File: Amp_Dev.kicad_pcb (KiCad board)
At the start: 2 copper layers, 100 x 100 mm, 86 parts, among them J1 SMA, J10 SMA, J11 CONN_01X02, J13 SMA, J2 SMA, J20 SMA, J21 SMA, J22 SMA, Q1 DMN2075U, U1 MML09211H, U4 SN74LVC1G17, U5 TLV702, U6 LTC2644, U7 RT9183

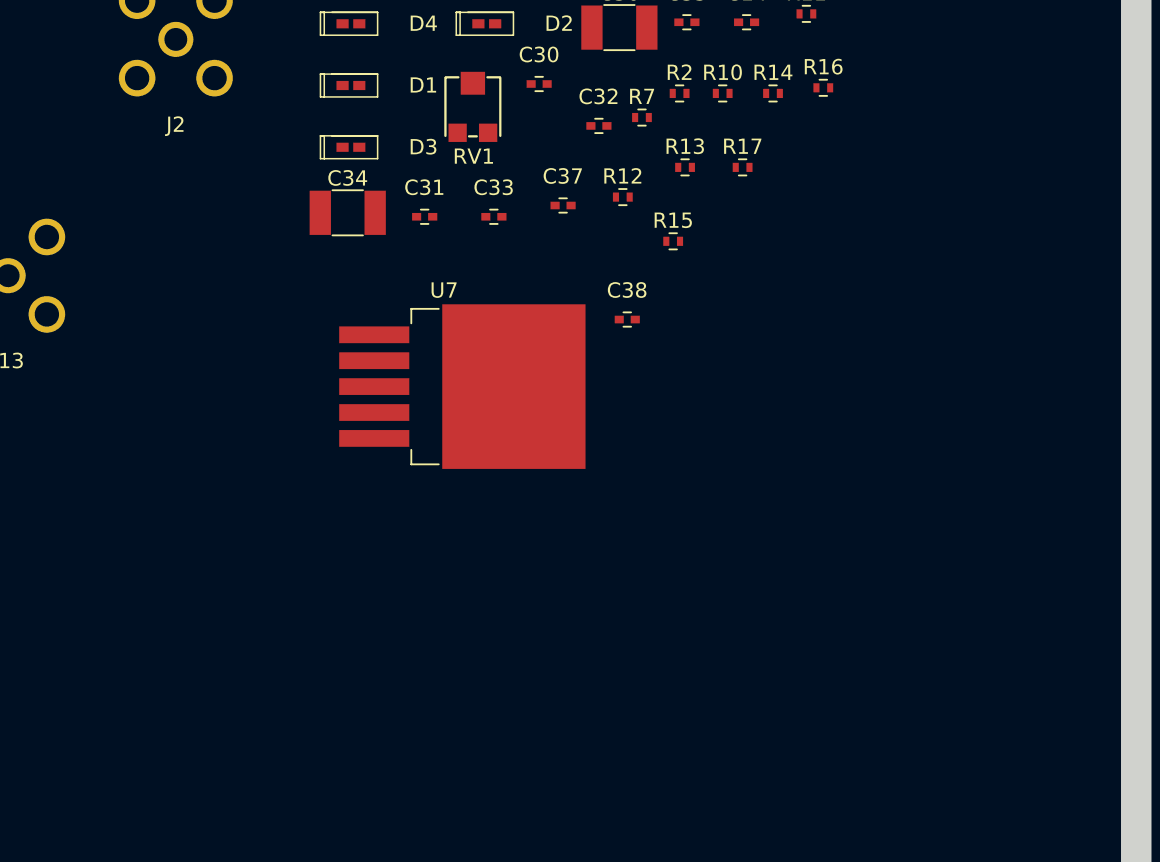
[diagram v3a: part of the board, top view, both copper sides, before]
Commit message: Forward annotated more PA components
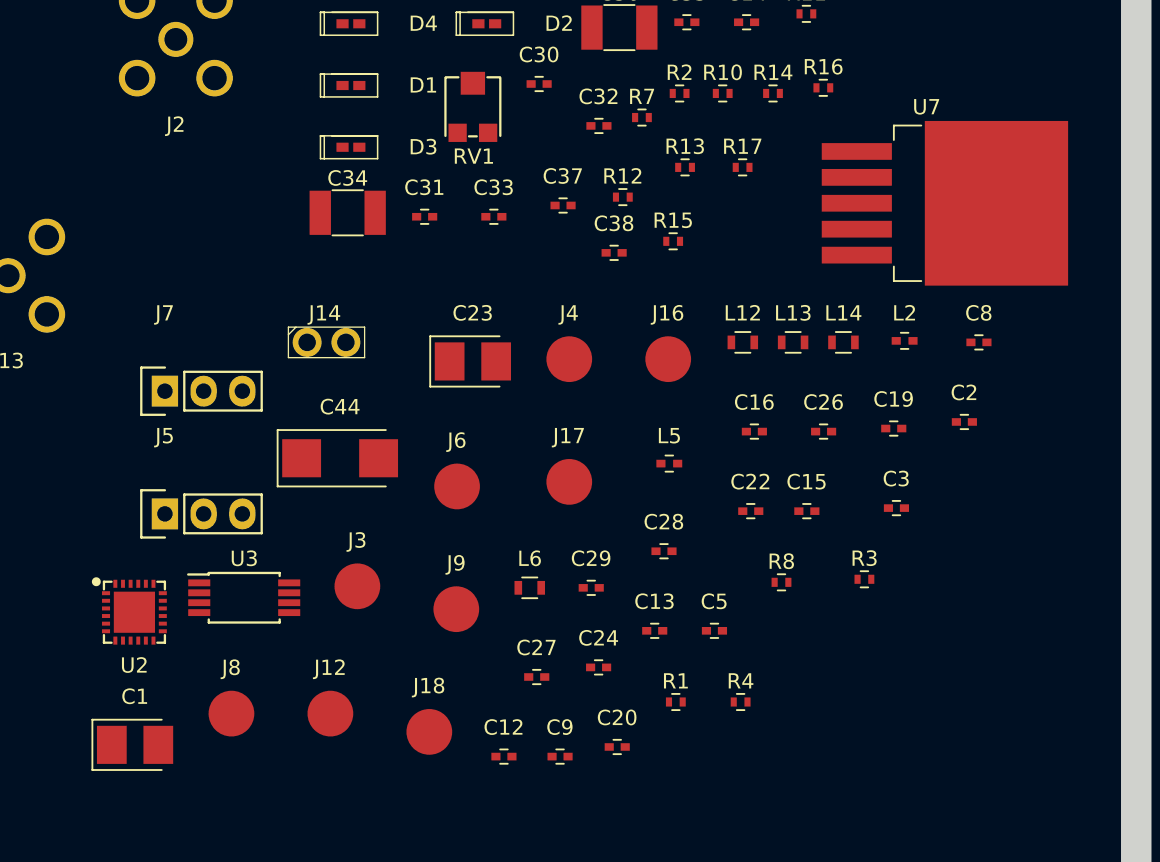
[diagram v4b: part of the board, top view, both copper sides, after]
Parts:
- added C1: 10uF, SFUSat:CP_Tantalum_Case-B_EIA-1411-21_Reflow, F.Cu at (134.3, 102.0)
- added C12: 1uF, SFUSat:C_0402, F.Cu at (158.5, 102.8)
- added C13: 1uF, SFUSat:C_0402, F.Cu at (168.4, 94.5)
- added C15: 1uF, SFUSat:C_0402, F.Cu at (178.4, 86.7)
- added C16: 2.2uF, SFUSat:C_0402, F.Cu at (175.0, 81.5)
- added C19: 1uF, SFUSat:C_0402, F.Cu at (184.1, 81.3)
- added C2: 1uF, SFUSat:C_0402, F.Cu at (188.7, 80.8)
- added C20: DNP, SFUSat:C_0402, F.Cu at (166.0, 102.2)
- added C22: 10pF, SFUSat:C_0402, F.Cu at (174.7, 86.7)
- added C23: 10uF, SFUSat:CP_Tantalum_Case-B_EIA-1411-21_Reflow, F.Cu at (156.5, 76.9)
- added C24: 27pF, SFUSat:C_0402, F.Cu at (164.7, 96.9)
- added C26: 2.2uF, SFUSat:C_0402, F.Cu at (179.5, 81.5)
- added C27: 10pF, SFUSat:C_0402, F.Cu at (160.7, 97.6)
- added C28: 1.2pF, SFUSat:C_0402, F.Cu at (169.0, 89.3)
- added C29: 100pF, SFUSat:C_0402, F.Cu at (164.2, 91.7)
- added C3: 100pF, SFUSat:C_0402, F.Cu at (184.3, 86.5)
- added C44: 10uF, SFUSat:CP_Tantalum_Case-C_EIA-2312-28_Reflow, F.Cu at (147.8, 83.2)
- added C5: 2.2uF, SFUSat:C_0402, F.Cu at (172.3, 94.5)
- added C8: 220pF, SFUSat:C_0402, F.Cu at (189.7, 75.6)
- added C9: 22pF, SFUSat:C_0402, F.Cu at (162.2, 102.8)
- added J12: TEST_1P, SFUSat:Measurement_Point_Round-SMD-Pad_Big, F.Cu at (147.1, 100.0)
- added J14: CONN_01X02, SFUSat:2x01In_Header_v2, F.Cu at (146.9, 75.6)
- added J16: TEST_1P, SFUSat:Measurement_Point_Round-SMD-Pad_Big, F.Cu at (169.3, 76.7)
- added J17: TEST_1P, SFUSat:Measurement_Point_Round-SMD-Pad_Big, F.Cu at (162.8, 84.8)
- added J18: TEST_1P, SFUSat:Measurement_Point_Round-SMD-Pad_Big, F.Cu at (153.6, 101.2)
- added J3: TEST_1P, SFUSat:Measurement_Point_Round-SMD-Pad_Big, F.Cu at (148.9, 91.6)
- added J4: TEST_1P, SFUSat:Measurement_Point_Round-SMD-Pad_Big, F.Cu at (162.8, 76.7)
- added J5: CONN_01X03, SFUSat:Socket_Strip_Straight_1x03, F.Cu at (136.3, 86.9)
- added J6: TEST_1P, SFUSat:Measurement_Point_Round-SMD-Pad_Big, F.Cu at (155.4, 85.1)
- added J7: CONN_01X03, SFUSat:Socket_Strip_Straight_1x03, F.Cu at (136.3, 78.8)
- added J8: TEST_1P, SFUSat:Measurement_Point_Round-SMD-Pad_Big, F.Cu at (140.6, 100.0)
- added J9: TEST_1P, SFUSat:Measurement_Point_Round-SMD-Pad_Big, F.Cu at (155.4, 93.1)
- added L12: 0R0, SFUSat:L_0603, F.Cu at (174.2, 75.6)
- added L13: 0R0, SFUSat:L_0603, F.Cu at (177.5, 75.6)
- added L14: 0R0, SFUSat:L_0603, F.Cu at (180.8, 75.6)
- added L2: 8.2nH, SFUSat:L_0402, F.Cu at (184.8, 75.5)
- added L5: 12.55nH, SFUSat:L_0402, F.Cu at (169.4, 83.6)
- added L6: L, SFUSat:L_0603, F.Cu at (160.2, 91.7)
- added R1: 220R, SFUSat:R_0402, F.Cu at (169.8, 99.2)
- added R3: 390R, SFUSat:R_0402, F.Cu at (182.2, 91.2)
- added R4: 390R, SFUSat:R_0402, F.Cu at (174.0, 99.2)
- added R8: 220R, SFUSat:R_0402, F.Cu at (176.7, 91.4)
- added U2: RF6886, SFUSat:QFN-24, F.Cu at (134.3, 93.3)
- added U3: LMV358, SFUSat:TSSOP-8_4.4x3mm_Pitch0.65mm, F.Cu at (141.5, 92.4)
- moved U7 33.9 mm to (186.2, 66.5)
- moved C38 4.46 mm to (165.8, 69.8)
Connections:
- C36 pad 1: Net-(C36-Pad1) -> /3V6
- R16 pad 1: Net-(C36-Pad1) -> /3V6
- U7 pad 4: Net-(C36-Pad1) -> /3V6

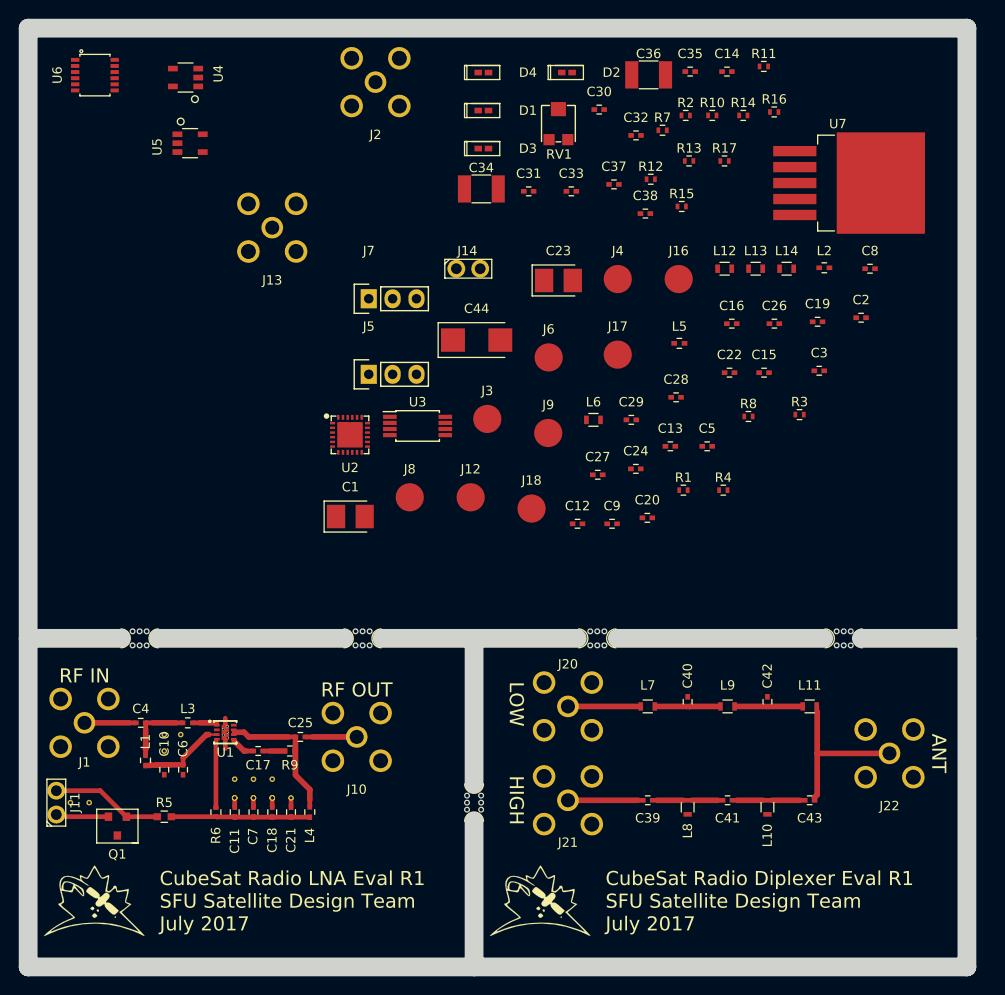
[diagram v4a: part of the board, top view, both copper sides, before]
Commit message: Routed PA power board
Sch:
-For LF, made L6 an 0603 0 ohm resistor like L12, L13, and L14
-Changed net 3.1V to 3V1

Layout:
-Routed all signals
-Added 1.5 cm spaced via fence around all boards (~1/20 wavelength)
-Fixed unconnected nets
-Added some silkscreen labels
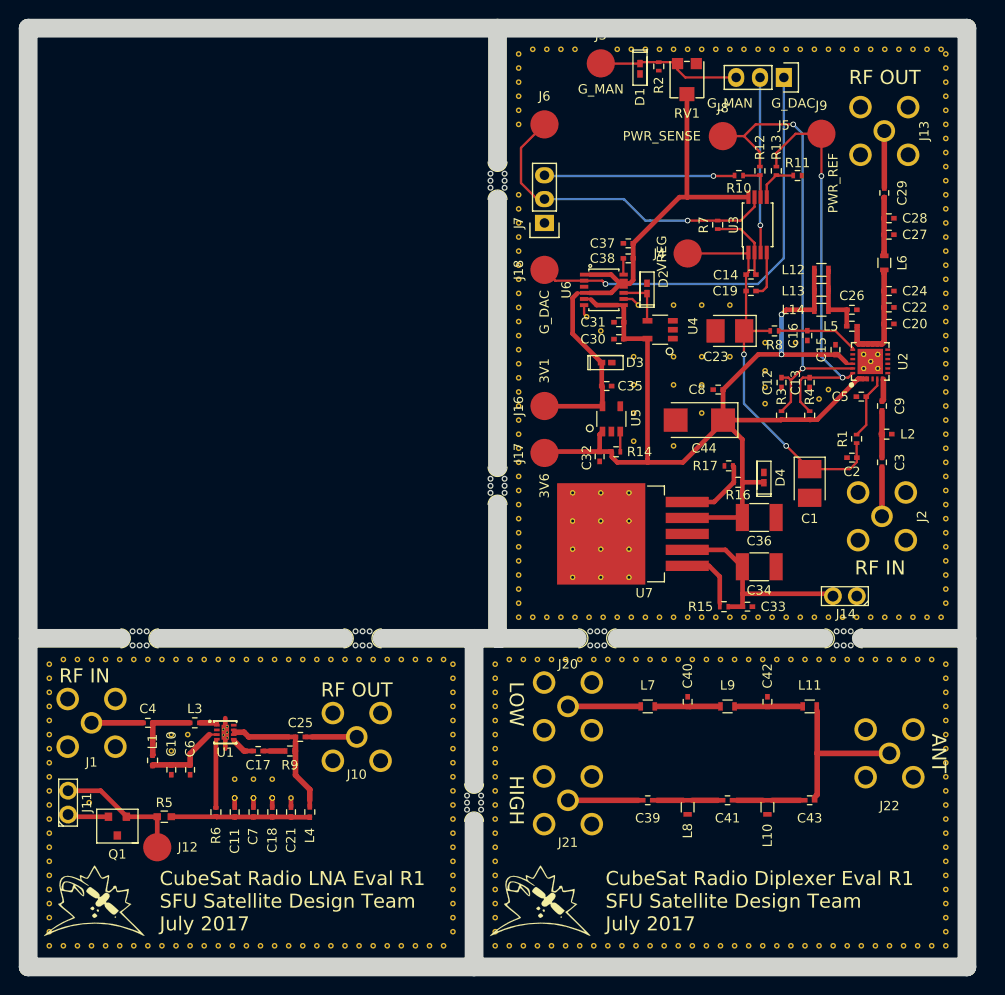
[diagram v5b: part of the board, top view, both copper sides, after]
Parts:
- removed the REF** at (104.5, 132.5)
- added REF**: VIA-0.6mm, SFUSat:VIA-0.6mm, F.Cu at (164.5, 94.0)
- added REF**: VIA-0.6mm, SFUSat:VIA-0.6mm, F.Cu at (171.8, 85.0)
- added REF**: VIA-0.6mm, SFUSat:VIA-0.6mm, F.Cu at (176.8, 147.8)
- added REF**: VIA-0.6mm, SFUSat:VIA-0.6mm, F.Cu at (175.2, 147.8)
- added REF**: VIA-0.6mm, SFUSat:VIA-0.6mm, F.Cu at (173.8, 147.8)
- added REF**: VIA-0.6mm, SFUSat:VIA-0.6mm, F.Cu at (172.2, 147.8)
- added REF**: VIA-0.6mm, SFUSat:VIA-0.6mm, F.Cu at (170.8, 147.8)
- added REF**: VIA-0.6mm, SFUSat:VIA-0.6mm, F.Cu at (169.2, 147.8)
- added REF**: VIA-0.6mm, SFUSat:VIA-0.6mm, F.Cu at (167.8, 147.8)
- added REF**: VIA-0.6mm, SFUSat:VIA-0.6mm, F.Cu at (166.2, 147.8)
- added REF**: VIA-0.6mm, SFUSat:VIA-0.6mm, F.Cu at (164.8, 147.8)
- added REF**: VIA-0.6mm, SFUSat:VIA-0.6mm, F.Cu at (163.2, 147.8)
- added REF**: VIA-0.6mm, SFUSat:VIA-0.6mm, F.Cu at (174.8, 85.0)
- added REF**: VIA-0.6mm, SFUSat:VIA-0.6mm, F.Cu at (161.8, 147.8)
- added REF**: VIA-0.6mm, SFUSat:VIA-0.6mm, F.Cu at (160.2, 147.8)
- added REF**: VIA-0.6mm, SFUSat:VIA-0.6mm, F.Cu at (158.8, 147.8)
- added REF**: VIA-0.6mm, SFUSat:VIA-0.6mm, F.Cu at (157.2, 147.8)
- added REF**: VIA-0.6mm, SFUSat:VIA-0.6mm, F.Cu at (155.8, 147.8)
- added REF**: VIA-0.6mm, SFUSat:VIA-0.6mm, F.Cu at (154.2, 147.8)
- added REF**: VIA-0.6mm, SFUSat:VIA-0.6mm, F.Cu at (152.8, 147.8)
- added REF**: VIA-0.6mm, SFUSat:VIA-0.6mm, F.Cu at (151.2, 147.8)
- added REF**: VIA-0.6mm, SFUSat:VIA-0.6mm, F.Cu at (149.8, 117.8)
- added REF**: VIA-0.6mm, SFUSat:VIA-0.6mm, F.Cu at (149.8, 119.2)
- added REF**: VIA-0.6mm, SFUSat:VIA-0.6mm, F.Cu at (168.8, 85.0)
- added REF**: VIA-0.6mm, SFUSat:VIA-0.6mm, F.Cu at (149.8, 120.8)
- added REF**: VIA-0.6mm, SFUSat:VIA-0.6mm, F.Cu at (149.8, 122.2)
- added REF**: VIA-0.6mm, SFUSat:VIA-0.6mm, F.Cu at (149.8, 123.8)
- added REF**: VIA-0.6mm, SFUSat:VIA-0.6mm, F.Cu at (149.8, 125.2)
- added REF**: VIA-0.6mm, SFUSat:VIA-0.6mm, F.Cu at (149.8, 126.8)
- added REF**: VIA-0.6mm, SFUSat:VIA-0.6mm, F.Cu at (149.8, 128.2)
- added REF**: VIA-0.6mm, SFUSat:VIA-0.6mm, F.Cu at (149.8, 129.8)
- added REF**: VIA-0.6mm, SFUSat:VIA-0.6mm, F.Cu at (149.8, 131.2)
- added REF**: VIA-0.6mm, SFUSat:VIA-0.6mm, F.Cu at (149.8, 132.8)
- added REF**: VIA-0.6mm, SFUSat:VIA-0.6mm, F.Cu at (149.8, 134.2)
- added REF**: VIA-0.6mm, SFUSat:VIA-0.6mm, F.Cu at (174.8, 79.5)
- added REF**: VIA-0.6mm, SFUSat:VIA-0.6mm, F.Cu at (149.8, 135.8)
- added REF**: VIA-0.6mm, SFUSat:VIA-0.6mm, F.Cu at (149.8, 137.2)
- added REF**: VIA-0.6mm, SFUSat:VIA-0.6mm, F.Cu at (149.8, 138.8)
- added REF**: VIA-0.6mm, SFUSat:VIA-0.6mm, F.Cu at (149.8, 140.2)
- added REF**: VIA-0.6mm, SFUSat:VIA-0.6mm, F.Cu at (149.8, 141.8)
- added REF**: VIA-0.6mm, SFUSat:VIA-0.6mm, F.Cu at (149.8, 143.2)
- added REF**: VIA-0.6mm, SFUSat:VIA-0.6mm, F.Cu at (149.8, 144.8)
- added REF**: VIA-0.6mm, SFUSat:VIA-0.6mm, F.Cu at (149.8, 146.2)
- added REF**: VIA-0.6mm, SFUSat:VIA-0.6mm, F.Cu at (149.8, 147.8)
- added REF**: VIA-0.6mm, SFUSat:VIA-0.6mm, F.Cu at (145.2, 117.8)
- added REF**: VIA-0.6mm, SFUSat:VIA-0.6mm, F.Cu at (171.8, 79.5)
- added REF**: VIA-0.6mm, SFUSat:VIA-0.6mm, F.Cu at (145.2, 119.2)
- added REF**: VIA-0.6mm, SFUSat:VIA-0.6mm, F.Cu at (145.2, 120.8)
- added REF**: VIA-0.6mm, SFUSat:VIA-0.6mm, F.Cu at (145.2, 122.2)
- added REF**: VIA-0.6mm, SFUSat:VIA-0.6mm, F.Cu at (145.2, 123.8)
- added REF**: VIA-0.6mm, SFUSat:VIA-0.6mm, F.Cu at (145.2, 125.2)
- added REF**: VIA-0.6mm, SFUSat:VIA-0.6mm, F.Cu at (145.2, 126.8)
- added REF**: VIA-0.6mm, SFUSat:VIA-0.6mm, F.Cu at (145.2, 128.2)
- added REF**: VIA-0.6mm, SFUSat:VIA-0.6mm, F.Cu at (145.2, 129.8)
- added REF**: VIA-0.6mm, SFUSat:VIA-0.6mm, F.Cu at (145.2, 131.2)
- added REF**: VIA-0.6mm, SFUSat:VIA-0.6mm, F.Cu at (145.2, 132.8)
- added REF**: VIA-0.6mm, SFUSat:VIA-0.6mm, F.Cu at (168.8, 79.5)
- added REF**: VIA-0.6mm, SFUSat:VIA-0.6mm, F.Cu at (145.2, 134.2)
- added REF**: VIA-0.6mm, SFUSat:VIA-0.6mm, F.Cu at (145.2, 135.8)
- added REF**: VIA-0.6mm, SFUSat:VIA-0.6mm, F.Cu at (145.2, 137.2)
- added REF**: VIA-0.6mm, SFUSat:VIA-0.6mm, F.Cu at (145.2, 138.8)
- added REF**: VIA-0.6mm, SFUSat:VIA-0.6mm, F.Cu at (145.2, 140.2)
- added REF**: VIA-0.6mm, SFUSat:VIA-0.6mm, F.Cu at (145.2, 141.8)
- added REF**: VIA-0.6mm, SFUSat:VIA-0.6mm, F.Cu at (145.2, 143.2)
- added REF**: VIA-0.6mm, SFUSat:VIA-0.6mm, F.Cu at (145.2, 144.8)
- added REF**: VIA-0.6mm, SFUSat:VIA-0.6mm, F.Cu at (145.2, 146.2)
- added REF**: VIA-0.6mm, SFUSat:VIA-0.6mm, F.Cu at (144.2, 117.2)
- added REF**: VIA-0.6mm, SFUSat:VIA-0.6mm, F.Cu at (159.5, 80.8)
- added REF**: VIA-0.6mm, SFUSat:VIA-0.6mm, F.Cu at (142.8, 117.2)
- added REF**: VIA-0.6mm, SFUSat:VIA-0.6mm, F.Cu at (141.2, 117.2)
- added REF**: VIA-0.6mm, SFUSat:VIA-0.6mm, F.Cu at (139.8, 117.2)
- added REF**: VIA-0.6mm, SFUSat:VIA-0.6mm, F.Cu at (138.2, 117.2)
- added REF**: VIA-0.6mm, SFUSat:VIA-0.6mm, F.Cu at (136.8, 117.2)
- added REF**: VIA-0.6mm, SFUSat:VIA-0.6mm, F.Cu at (135.2, 117.2)
- added REF**: VIA-0.6mm, SFUSat:VIA-0.6mm, F.Cu at (133.8, 117.2)
- added REF**: VIA-0.6mm, SFUSat:VIA-0.6mm, F.Cu at (132.2, 117.2)
- added REF**: VIA-0.6mm, SFUSat:VIA-0.6mm, F.Cu at (130.8, 117.2)
- added REF**: VIA-0.6mm, SFUSat:VIA-0.6mm, F.Cu at (129.2, 117.2)
- added REF**: VIA-0.6mm, SFUSat:VIA-0.6mm, F.Cu at (164.0, 108.5)
- added REF**: VIA-0.6mm, SFUSat:VIA-0.6mm, F.Cu at (127.8, 117.2)
- added REF**: VIA-0.6mm, SFUSat:VIA-0.6mm, F.Cu at (126.2, 117.2)
- added REF**: VIA-0.6mm, SFUSat:VIA-0.6mm, F.Cu at (124.8, 117.2)
- added REF**: VIA-0.6mm, SFUSat:VIA-0.6mm, F.Cu at (123.2, 117.2)
- added REF**: VIA-0.6mm, SFUSat:VIA-0.6mm, F.Cu at (121.8, 117.2)
- added REF**: VIA-0.6mm, SFUSat:VIA-0.6mm, F.Cu at (120.2, 117.2)
- added REF**: VIA-0.6mm, SFUSat:VIA-0.6mm, F.Cu at (118.8, 117.2)
- added REF**: VIA-0.6mm, SFUSat:VIA-0.6mm, F.Cu at (117.2, 117.2)
- added REF**: VIA-0.6mm, SFUSat:VIA-0.6mm, F.Cu at (115.8, 117.2)
- added REF**: VIA-0.6mm, SFUSat:VIA-0.6mm, F.Cu at (114.2, 117.2)
- added REF**: VIA-0.6mm, SFUSat:VIA-0.6mm, F.Cu at (161.0, 108.5)
- added REF**: VIA-0.6mm, SFUSat:VIA-0.6mm, F.Cu at (112.8, 117.2)
- added REF**: VIA-0.6mm, SFUSat:VIA-0.6mm, F.Cu at (111.2, 117.2)
- added REF**: VIA-0.6mm, SFUSat:VIA-0.6mm, F.Cu at (109.8, 117.2)
- added REF**: VIA-0.6mm, SFUSat:VIA-0.6mm, F.Cu at (108.2, 117.2)
- added REF**: VIA-0.6mm, SFUSat:VIA-0.6mm, F.Cu at (106.8, 117.2)
- added REF**: VIA-0.6mm, SFUSat:VIA-0.6mm, F.Cu at (105.2, 117.2)
- added REF**: VIA-0.6mm, SFUSat:VIA-0.6mm, F.Cu at (103.8, 117.2)
- added REF**: VIA-0.6mm, SFUSat:VIA-0.6mm, F.Cu at (102.2, 117.8)
- added REF**: VIA-0.6mm, SFUSat:VIA-0.6mm, F.Cu at (102.2, 119.2)
- added REF**: VIA-0.6mm, SFUSat:VIA-0.6mm, F.Cu at (102.2, 120.8)
- added REF**: VIA-0.6mm, SFUSat:VIA-0.6mm, F.Cu at (158.0, 108.5)
- added REF**: VIA-0.6mm, SFUSat:VIA-0.6mm, F.Cu at (102.2, 122.2)
- added REF**: VIA-0.6mm, SFUSat:VIA-0.6mm, F.Cu at (102.2, 123.8)
- added REF**: VIA-0.6mm, SFUSat:VIA-0.6mm, F.Cu at (102.2, 125.2)
- added REF**: VIA-0.6mm, SFUSat:VIA-0.6mm, F.Cu at (102.2, 126.8)
- added REF**: VIA-0.6mm, SFUSat:VIA-0.6mm, F.Cu at (102.2, 128.2)
- added REF**: VIA-0.6mm, SFUSat:VIA-0.6mm, F.Cu at (102.2, 129.8)
- added REF**: VIA-0.6mm, SFUSat:VIA-0.6mm, F.Cu at (102.2, 131.2)
- added REF**: VIA-0.6mm, SFUSat:VIA-0.6mm, F.Cu at (102.2, 132.8)
- added REF**: VIA-0.6mm, SFUSat:VIA-0.6mm, F.Cu at (102.2, 134.2)
- added REF**: VIA-0.6mm, SFUSat:VIA-0.6mm, F.Cu at (102.2, 135.8)
- added REF**: VIA-0.6mm, SFUSat:VIA-0.6mm, F.Cu at (164.5, 91.0)
- added REF**: VIA-0.6mm, SFUSat:VIA-0.6mm, F.Cu at (164.0, 105.5)
- added REF**: VIA-0.6mm, SFUSat:VIA-0.6mm, F.Cu at (102.2, 137.2)
- added REF**: VIA-0.6mm, SFUSat:VIA-0.6mm, F.Cu at (102.2, 138.8)
- added REF**: VIA-0.6mm, SFUSat:VIA-0.6mm, F.Cu at (102.2, 140.2)
- added REF**: VIA-0.6mm, SFUSat:VIA-0.6mm, F.Cu at (102.2, 141.8)
- added REF**: VIA-0.6mm, SFUSat:VIA-0.6mm, F.Cu at (102.2, 143.2)
- added REF**: VIA-0.6mm, SFUSat:VIA-0.6mm, F.Cu at (102.2, 144.8)
- added REF**: VIA-0.6mm, SFUSat:VIA-0.6mm, F.Cu at (102.2, 146.2)
- added REF**: VIA-0.6mm, SFUSat:VIA-0.6mm, F.Cu at (144.2, 147.8)
- added REF**: VIA-0.6mm, SFUSat:VIA-0.6mm, F.Cu at (142.8, 147.8)
- added REF**: VIA-0.6mm, SFUSat:VIA-0.6mm, F.Cu at (141.2, 147.8)
- added REF**: VIA-0.6mm, SFUSat:VIA-0.6mm, F.Cu at (161.0, 105.5)
- added REF**: VIA-0.6mm, SFUSat:VIA-0.6mm, F.Cu at (139.8, 147.8)
- added REF**: VIA-0.6mm, SFUSat:VIA-0.6mm, F.Cu at (138.2, 147.8)
- added REF**: VIA-0.6mm, SFUSat:VIA-0.6mm, F.Cu at (136.8, 147.8)
- added REF**: VIA-0.6mm, SFUSat:VIA-0.6mm, F.Cu at (135.2, 147.8)
- added REF**: VIA-0.6mm, SFUSat:VIA-0.6mm, F.Cu at (133.8, 147.8)
- added REF**: VIA-0.6mm, SFUSat:VIA-0.6mm, F.Cu at (132.2, 147.8)
- added REF**: VIA-0.6mm, SFUSat:VIA-0.6mm, F.Cu at (130.8, 147.8)
- added REF**: VIA-0.6mm, SFUSat:VIA-0.6mm, F.Cu at (129.2, 147.8)
- added REF**: VIA-0.6mm, SFUSat:VIA-0.6mm, F.Cu at (127.8, 147.8)
- added REF**: VIA-0.6mm, SFUSat:VIA-0.6mm, F.Cu at (126.2, 147.8)
- added REF**: VIA-0.6mm, SFUSat:VIA-0.6mm, F.Cu at (158.0, 105.5)
- added REF**: VIA-0.6mm, SFUSat:VIA-0.6mm, F.Cu at (124.8, 147.8)
- added REF**: VIA-0.6mm, SFUSat:VIA-0.6mm, F.Cu at (123.2, 147.8)
- added REF**: VIA-0.6mm, SFUSat:VIA-0.6mm, F.Cu at (121.8, 147.8)
- added REF**: VIA-0.6mm, SFUSat:VIA-0.6mm, F.Cu at (120.2, 147.8)
- added REF**: VIA-0.6mm, SFUSat:VIA-0.6mm, F.Cu at (118.8, 147.8)
- added REF**: VIA-0.6mm, SFUSat:VIA-0.6mm, F.Cu at (117.2, 147.8)
- added REF**: VIA-0.6mm, SFUSat:VIA-0.6mm, F.Cu at (115.8, 147.8)
- added REF**: VIA-0.6mm, SFUSat:VIA-0.6mm, F.Cu at (114.2, 147.8)
- added REF**: VIA-0.6mm, SFUSat:VIA-0.6mm, F.Cu at (112.8, 147.8)
- added REF**: VIA-0.6mm, SFUSat:VIA-0.6mm, F.Cu at (111.2, 147.8)
- added REF**: VIA-0.6mm, SFUSat:VIA-0.6mm, F.Cu at (164.0, 102.5)
- added REF**: VIA-0.6mm, SFUSat:VIA-0.6mm, F.Cu at (109.8, 147.8)
- added REF**: VIA-0.6mm, SFUSat:VIA-0.6mm, F.Cu at (108.2, 147.8)
- added REF**: VIA-0.6mm, SFUSat:VIA-0.6mm, F.Cu at (106.8, 147.8)
- added REF**: VIA-0.6mm, SFUSat:VIA-0.6mm, F.Cu at (105.2, 147.8)
- added REF**: VIA-0.6mm, SFUSat:VIA-0.6mm, F.Cu at (103.8, 147.8)
- added REF**: VIA-0.6mm, SFUSat:VIA-0.6mm, F.Cu at (102.2, 147.8)
- added REF**: VIA-0.6mm, SFUSat:VIA-0.6mm, F.Cu at (197.2, 52.2)
- added REF**: VIA-0.6mm, SFUSat:VIA-0.6mm, F.Cu at (195.8, 52.2)
- added REF**: VIA-0.6mm, SFUSat:VIA-0.6mm, F.Cu at (194.2, 52.2)
- added REF**: VIA-0.6mm, SFUSat:VIA-0.6mm, F.Cu at (192.8, 52.2)
- added REF**: VIA-0.6mm, SFUSat:VIA-0.6mm, F.Cu at (161.0, 102.5)
- added REF**: VIA-0.6mm, SFUSat:VIA-0.6mm, F.Cu at (191.2, 52.2)
- added REF**: VIA-0.6mm, SFUSat:VIA-0.6mm, F.Cu at (189.8, 52.2)
- added REF**: VIA-0.6mm, SFUSat:VIA-0.6mm, F.Cu at (188.2, 52.2)
- added REF**: VIA-0.6mm, SFUSat:VIA-0.6mm, F.Cu at (186.8, 52.2)
- added REF**: VIA-0.6mm, SFUSat:VIA-0.6mm, F.Cu at (185.2, 52.2)
- added REF**: VIA-0.6mm, SFUSat:VIA-0.6mm, F.Cu at (183.8, 52.2)
- added REF**: VIA-0.6mm, SFUSat:VIA-0.6mm, F.Cu at (182.2, 52.2)
- added REF**: VIA-0.6mm, SFUSat:VIA-0.6mm, F.Cu at (180.8, 52.2)
- added REF**: VIA-0.6mm, SFUSat:VIA-0.6mm, F.Cu at (179.2, 52.2)
- added REF**: VIA-0.6mm, SFUSat:VIA-0.6mm, F.Cu at (177.8, 52.2)
- added REF**: VIA-0.6mm, SFUSat:VIA-0.6mm, F.Cu at (158.0, 102.5)
- added REF**: VIA-0.6mm, SFUSat:VIA-0.6mm, F.Cu at (176.2, 52.2)
- added REF**: VIA-0.6mm, SFUSat:VIA-0.6mm, F.Cu at (174.8, 52.2)
- added REF**: VIA-0.6mm, SFUSat:VIA-0.6mm, F.Cu at (173.2, 52.2)
- added REF**: VIA-0.6mm, SFUSat:VIA-0.6mm, F.Cu at (171.8, 52.2)
- added REF**: VIA-0.6mm, SFUSat:VIA-0.6mm, F.Cu at (170.2, 52.2)
- added REF**: VIA-0.6mm, SFUSat:VIA-0.6mm, F.Cu at (168.8, 52.2)
- added REF**: VIA-0.6mm, SFUSat:VIA-0.6mm, F.Cu at (167.2, 52.2)
- added REF**: VIA-0.6mm, SFUSat:VIA-0.6mm, F.Cu at (165.8, 52.2)
- added REF**: VIA-0.6mm, SFUSat:VIA-0.6mm, F.Cu at (164.2, 52.2)
- added REF**: VIA-0.6mm, SFUSat:VIA-0.6mm, F.Cu at (162.8, 52.2)
- added REF**: VIA-0.6mm, SFUSat:VIA-0.6mm, F.Cu at (164.0, 99.5)
- added REF**: VIA-0.6mm, SFUSat:VIA-0.6mm, F.Cu at (158.2, 52.2)
- added REF**: VIA-0.6mm, SFUSat:VIA-0.6mm, F.Cu at (156.8, 52.2)
- added REF**: VIA-0.6mm, SFUSat:VIA-0.6mm, F.Cu at (155.2, 52.2)
- added REF**: VIA-0.6mm, SFUSat:VIA-0.6mm, F.Cu at (153.8, 52.2)
- added REF**: VIA-0.6mm, SFUSat:VIA-0.6mm, F.Cu at (197.8, 52.8)
- added REF**: VIA-0.6mm, SFUSat:VIA-0.6mm, F.Cu at (197.8, 54.2)
- added REF**: VIA-0.6mm, SFUSat:VIA-0.6mm, F.Cu at (197.8, 55.8)
- added REF**: VIA-0.6mm, SFUSat:VIA-0.6mm, F.Cu at (197.8, 57.2)
- added REF**: VIA-0.6mm, SFUSat:VIA-0.6mm, F.Cu at (197.8, 58.8)
- added REF**: VIA-0.6mm, SFUSat:VIA-0.6mm, F.Cu at (197.8, 60.2)
- added REF**: VIA-0.6mm, SFUSat:VIA-0.6mm, F.Cu at (161.0, 99.5)
- added REF**: VIA-0.6mm, SFUSat:VIA-0.6mm, F.Cu at (197.8, 61.8)
- added REF**: VIA-0.6mm, SFUSat:VIA-0.6mm, F.Cu at (197.8, 63.2)
- added REF**: VIA-0.6mm, SFUSat:VIA-0.6mm, F.Cu at (197.8, 64.8)
- added REF**: VIA-0.6mm, SFUSat:VIA-0.6mm, F.Cu at (197.8, 66.2)
- added REF**: VIA-0.6mm, SFUSat:VIA-0.6mm, F.Cu at (197.8, 67.8)
- added REF**: VIA-0.6mm, SFUSat:VIA-0.6mm, F.Cu at (197.8, 69.2)
- added REF**: VIA-0.6mm, SFUSat:VIA-0.6mm, F.Cu at (197.8, 70.8)
- added REF**: VIA-0.6mm, SFUSat:VIA-0.6mm, F.Cu at (197.8, 72.2)
- added REF**: VIA-0.6mm, SFUSat:VIA-0.6mm, F.Cu at (197.8, 73.8)
- added REF**: VIA-0.6mm, SFUSat:VIA-0.6mm, F.Cu at (197.8, 75.2)
- added REF**: VIA-0.6mm, SFUSat:VIA-0.6mm, F.Cu at (158.0, 99.5)
- added REF**: VIA-0.6mm, SFUSat:VIA-0.6mm, F.Cu at (197.8, 76.8)
- added REF**: VIA-0.6mm, SFUSat:VIA-0.6mm, F.Cu at (197.8, 78.2)
- added REF**: VIA-0.6mm, SFUSat:VIA-0.6mm, F.Cu at (197.8, 79.8)
- added REF**: VIA-0.6mm, SFUSat:VIA-0.6mm, F.Cu at (197.8, 81.2)
- added REF**: VIA-0.6mm, SFUSat:VIA-0.6mm, F.Cu at (197.8, 82.8)
- added REF**: VIA-0.6mm, SFUSat:VIA-0.6mm, F.Cu at (197.8, 84.2)
- added REF**: VIA-0.6mm, SFUSat:VIA-0.6mm, F.Cu at (197.8, 85.8)
- added REF**: VIA-0.6mm, SFUSat:VIA-0.6mm, F.Cu at (197.8, 87.2)
- added REF**: VIA-0.6mm, SFUSat:VIA-0.6mm, F.Cu at (197.8, 88.8)
- added REF**: VIA-0.6mm, SFUSat:VIA-0.6mm, F.Cu at (197.8, 90.2)
- added REF**: VIA-0.6mm, SFUSat:VIA-0.6mm, F.Cu at (181.8, 83.5)
- added REF**: VIA-0.6mm, SFUSat:VIA-0.6mm, F.Cu at (197.8, 91.8)
- added REF**: VIA-0.6mm, SFUSat:VIA-0.6mm, F.Cu at (197.8, 93.2)
- added REF**: VIA-0.6mm, SFUSat:VIA-0.6mm, F.Cu at (197.8, 94.8)
- added REF**: VIA-0.6mm, SFUSat:VIA-0.6mm, F.Cu at (197.8, 96.2)
- added REF**: VIA-0.6mm, SFUSat:VIA-0.6mm, F.Cu at (197.8, 97.8)
- added REF**: VIA-0.6mm, SFUSat:VIA-0.6mm, F.Cu at (197.8, 99.2)
- added REF**: VIA-0.6mm, SFUSat:VIA-0.6mm, F.Cu at (197.8, 100.8)
- added REF**: VIA-0.6mm, SFUSat:VIA-0.6mm, F.Cu at (197.8, 102.2)
- added REF**: VIA-0.6mm, SFUSat:VIA-0.6mm, F.Cu at (197.8, 103.8)
- added REF**: VIA-0.6mm, SFUSat:VIA-0.6mm, F.Cu at (197.8, 105.2)
- added REF**: VIA-0.6mm, SFUSat:VIA-0.6mm, F.Cu at (164.5, 88.0)
- added REF**: VIA-0.6mm, SFUSat:VIA-0.6mm, F.Cu at (178.5, 83.5)
- added REF**: VIA-0.6mm, SFUSat:VIA-0.6mm, F.Cu at (197.8, 106.8)
- added REF**: VIA-0.6mm, SFUSat:VIA-0.6mm, F.Cu at (197.8, 108.2)
- added REF**: VIA-0.6mm, SFUSat:VIA-0.6mm, F.Cu at (197.8, 109.8)
- added REF**: VIA-0.6mm, SFUSat:VIA-0.6mm, F.Cu at (197.8, 111.2)
- added REF**: VIA-0.6mm, SFUSat:VIA-0.6mm, F.Cu at (197.2, 112.8)
- added REF**: VIA-0.6mm, SFUSat:VIA-0.6mm, F.Cu at (195.8, 112.8)
- added REF**: VIA-0.6mm, SFUSat:VIA-0.6mm, F.Cu at (194.2, 112.8)
- added REF**: VIA-0.6mm, SFUSat:VIA-0.6mm, F.Cu at (192.8, 112.8)
- added REF**: VIA-0.6mm, SFUSat:VIA-0.6mm, F.Cu at (191.2, 112.8)
- added REF**: VIA-0.6mm, SFUSat:VIA-0.6mm, F.Cu at (189.8, 112.8)
- added REF**: VIA-0.6mm, SFUSat:VIA-0.6mm, F.Cu at (184.2, 89.5)
- added REF**: VIA-0.6mm, SFUSat:VIA-0.6mm, F.Cu at (188.2, 112.8)
- added REF**: VIA-0.6mm, SFUSat:VIA-0.6mm, F.Cu at (186.8, 112.8)
- added REF**: VIA-0.6mm, SFUSat:VIA-0.6mm, F.Cu at (185.2, 112.8)
- added REF**: VIA-0.6mm, SFUSat:VIA-0.6mm, F.Cu at (183.8, 112.8)
- added REF**: VIA-0.6mm, SFUSat:VIA-0.6mm, F.Cu at (182.2, 112.8)
- added REF**: VIA-0.6mm, SFUSat:VIA-0.6mm, F.Cu at (180.8, 112.8)
- added REF**: VIA-0.6mm, SFUSat:VIA-0.6mm, F.Cu at (179.2, 112.8)
- added REF**: VIA-0.6mm, SFUSat:VIA-0.6mm, F.Cu at (177.8, 112.8)
- added REF**: VIA-0.6mm, SFUSat:VIA-0.6mm, F.Cu at (176.2, 112.8)
- added REF**: VIA-0.6mm, SFUSat:VIA-0.6mm, F.Cu at (174.8, 112.8)
- added REF**: VIA-0.6mm, SFUSat:VIA-0.6mm, F.Cu at (178.5, 86.5)
- added REF**: VIA-0.6mm, SFUSat:VIA-0.6mm, F.Cu at (173.2, 112.8)
- added REF**: VIA-0.6mm, SFUSat:VIA-0.6mm, F.Cu at (171.8, 112.8)
- added REF**: VIA-0.6mm, SFUSat:VIA-0.6mm, F.Cu at (170.2, 112.8)
- added REF**: VIA-0.6mm, SFUSat:VIA-0.6mm, F.Cu at (168.8, 112.8)
- added REF**: VIA-0.6mm, SFUSat:VIA-0.6mm, F.Cu at (167.2, 112.8)
- added REF**: VIA-0.6mm, SFUSat:VIA-0.6mm, F.Cu at (165.8, 112.8)
- added REF**: VIA-0.6mm, SFUSat:VIA-0.6mm, F.Cu at (164.2, 112.8)
- added REF**: VIA-0.6mm, SFUSat:VIA-0.6mm, F.Cu at (162.8, 112.8)
- added REF**: VIA-0.6mm, SFUSat:VIA-0.6mm, F.Cu at (161.2, 112.8)
- added REF**: VIA-0.6mm, SFUSat:VIA-0.6mm, F.Cu at (159.8, 112.8)
- added REF**: VIA-0.6mm, SFUSat:VIA-0.6mm, F.Cu at (178.5, 88.2)
- added REF**: VIA-0.6mm, SFUSat:VIA-0.6mm, F.Cu at (158.2, 112.8)
- added REF**: VIA-0.6mm, SFUSat:VIA-0.6mm, F.Cu at (156.8, 112.8)
- added REF**: VIA-0.6mm, SFUSat:VIA-0.6mm, F.Cu at (155.2, 112.8)
- added REF**: VIA-0.6mm, SFUSat:VIA-0.6mm, F.Cu at (153.8, 112.8)
- added REF**: VIA-0.6mm, SFUSat:VIA-0.6mm, F.Cu at (152.2, 52.8)
- added REF**: VIA-0.6mm, SFUSat:VIA-0.6mm, F.Cu at (152.2, 54.2)
- added REF**: VIA-0.6mm, SFUSat:VIA-0.6mm, F.Cu at (152.2, 55.8)
- added REF**: VIA-0.6mm, SFUSat:VIA-0.6mm, F.Cu at (152.2, 57.2)
- added REF**: VIA-0.6mm, SFUSat:VIA-0.6mm, F.Cu at (152.2, 58.8)
- added REF**: VIA-0.6mm, SFUSat:VIA-0.6mm, F.Cu at (152.2, 60.2)
- added REF**: VIA-0.6mm, SFUSat:VIA-0.6mm, F.Cu at (178.5, 90.0)
- added REF**: VIA-0.6mm, SFUSat:VIA-0.6mm, F.Cu at (152.2, 67.8)
- added REF**: VIA-0.6mm, SFUSat:VIA-0.6mm, F.Cu at (152.2, 69.2)
- added REF**: VIA-0.6mm, SFUSat:VIA-0.6mm, F.Cu at (152.2, 70.8)
- added REF**: VIA-0.6mm, SFUSat:VIA-0.6mm, F.Cu at (152.2, 72.2)
- added REF**: VIA-0.6mm, SFUSat:VIA-0.6mm, F.Cu at (152.2, 73.8)
- added REF**: VIA-0.6mm, SFUSat:VIA-0.6mm, F.Cu at (152.2, 75.2)
- added REF**: VIA-0.6mm, SFUSat:VIA-0.6mm, F.Cu at (152.2, 76.8)
- added REF**: VIA-0.6mm, SFUSat:VIA-0.6mm, F.Cu at (152.2, 78.2)
- added REF**: VIA-0.6mm, SFUSat:VIA-0.6mm, F.Cu at (152.2, 79.8)
- added REF**: VIA-0.6mm, SFUSat:VIA-0.6mm, F.Cu at (152.2, 81.2)
- added REF**: VIA-0.6mm, SFUSat:VIA-0.6mm, F.Cu at (196.2, 117.2)
- added REF**: VIA-0.6mm, SFUSat:VIA-0.6mm, F.Cu at (152.2, 82.8)
- added REF**: VIA-0.6mm, SFUSat:VIA-0.6mm, F.Cu at (152.2, 84.2)
- added REF**: VIA-0.6mm, SFUSat:VIA-0.6mm, F.Cu at (152.2, 85.8)
- added REF**: VIA-0.6mm, SFUSat:VIA-0.6mm, F.Cu at (152.2, 87.2)
- added REF**: VIA-0.6mm, SFUSat:VIA-0.6mm, F.Cu at (152.2, 88.8)
- added REF**: VIA-0.6mm, SFUSat:VIA-0.6mm, F.Cu at (152.2, 90.2)
- added REF**: VIA-0.6mm, SFUSat:VIA-0.6mm, F.Cu at (152.2, 91.8)
- added REF**: VIA-0.6mm, SFUSat:VIA-0.6mm, F.Cu at (152.2, 93.2)
- added REF**: VIA-0.6mm, SFUSat:VIA-0.6mm, F.Cu at (152.2, 94.8)
- added REF**: VIA-0.6mm, SFUSat:VIA-0.6mm, F.Cu at (152.2, 96.2)
- added REF**: VIA-0.6mm, SFUSat:VIA-0.6mm, F.Cu at (194.8, 117.2)
- added REF**: VIA-0.6mm, SFUSat:VIA-0.6mm, F.Cu at (152.2, 97.8)
- added REF**: VIA-0.6mm, SFUSat:VIA-0.6mm, F.Cu at (152.2, 99.2)
- added REF**: VIA-0.6mm, SFUSat:VIA-0.6mm, F.Cu at (152.2, 100.8)
- added REF**: VIA-0.6mm, SFUSat:VIA-0.6mm, F.Cu at (152.2, 102.2)
- added REF**: VIA-0.6mm, SFUSat:VIA-0.6mm, F.Cu at (152.2, 103.8)
- added REF**: VIA-0.6mm, SFUSat:VIA-0.6mm, F.Cu at (152.2, 105.2)
- added REF**: VIA-0.6mm, SFUSat:VIA-0.6mm, F.Cu at (152.2, 106.8)
- added REF**: VIA-0.6mm, SFUSat:VIA-0.6mm, F.Cu at (152.2, 108.2)
- added REF**: VIA-0.6mm, SFUSat:VIA-0.6mm, F.Cu at (152.2, 109.8)
- added REF**: VIA-0.6mm, SFUSat:VIA-0.6mm, F.Cu at (152.2, 111.2)
- added REF**: VIA-0.6mm, SFUSat:VIA-0.6mm, F.Cu at (193.2, 117.2)
- added REF**: VIA-0.6mm, SFUSat:VIA-0.6mm, F.Cu at (152.2, 112.8)
- added REF**: VIA-0.6mm, SFUSat:VIA-0.6mm, F.Cu at (165.0, 79.5)
- added REF**: VIA-0.6mm, SFUSat:VIA-0.6mm, F.Cu at (185.2, 88.5)
- added REF**: VIA-0.6mm, SFUSat:VIA-0.6mm, F.Cu at (189.8, 85.5)
- added REF**: VIA-0.6mm, SFUSat:VIA-0.6mm, F.Cu at (190.5, 84.8)
- added REF**: VIA-0.6mm, SFUSat:VIA-0.6mm, F.Cu at (190.5, 86.2)
- added REF**: VIA-0.6mm, SFUSat:VIA-0.6mm, F.Cu at (189.0, 86.2)
- added REF**: VIA-0.6mm, SFUSat:VIA-0.6mm, F.Cu at (189.0, 84.8)
- added REF**: VIA-0.6mm, SFUSat:VIA-0.6mm, F.Cu at (191.8, 117.2)
- added REF**: VIA-0.6mm, SFUSat:VIA-0.6mm, F.Cu at (190.2, 117.2)
- added REF**: VIA-0.6mm, SFUSat:VIA-0.6mm, F.Cu at (164.5, 85.0)
- added REF**: VIA-0.6mm, SFUSat:VIA-0.6mm, F.Cu at (188.8, 117.2)
- added REF**: VIA-0.6mm, SFUSat:VIA-0.6mm, F.Cu at (187.2, 117.2)
- added REF**: VIA-0.6mm, SFUSat:VIA-0.6mm, F.Cu at (185.8, 117.2)
- added REF**: VIA-0.6mm, SFUSat:VIA-0.6mm, F.Cu at (184.2, 117.2)
- added REF**: VIA-0.6mm, SFUSat:VIA-0.6mm, F.Cu at (182.8, 117.2)
- added REF**: VIA-0.6mm, SFUSat:VIA-0.6mm, F.Cu at (181.2, 117.2)
- added REF**: VIA-0.6mm, SFUSat:VIA-0.6mm, F.Cu at (179.8, 117.2)
- added REF**: VIA-0.6mm, SFUSat:VIA-0.6mm, F.Cu at (178.2, 117.2)
- added REF**: VIA-0.6mm, SFUSat:VIA-0.6mm, F.Cu at (176.8, 117.2)
- added REF**: VIA-0.6mm, SFUSat:VIA-0.6mm, F.Cu at (175.2, 117.2)
- added REF**: VIA-0.6mm, SFUSat:VIA-0.6mm, F.Cu at (161.0, 82.2)
- added REF**: VIA-0.6mm, SFUSat:VIA-0.6mm, F.Cu at (173.8, 117.2)
- added REF**: VIA-0.6mm, SFUSat:VIA-0.6mm, F.Cu at (172.2, 117.2)
- added REF**: VIA-0.6mm, SFUSat:VIA-0.6mm, F.Cu at (170.8, 117.2)
- added REF**: VIA-0.6mm, SFUSat:VIA-0.6mm, F.Cu at (169.2, 117.2)
- added REF**: VIA-0.6mm, SFUSat:VIA-0.6mm, F.Cu at (167.8, 117.2)
- added REF**: VIA-0.6mm, SFUSat:VIA-0.6mm, F.Cu at (166.2, 117.2)
- added REF**: VIA-0.6mm, SFUSat:VIA-0.6mm, F.Cu at (164.8, 117.2)
- added REF**: VIA-0.6mm, SFUSat:VIA-0.6mm, F.Cu at (163.2, 117.2)
- added REF**: VIA-0.6mm, SFUSat:VIA-0.6mm, F.Cu at (161.8, 117.2)
- added REF**: VIA-0.6mm, SFUSat:VIA-0.6mm, F.Cu at (160.2, 117.2)
- added REF**: VIA-0.6mm, SFUSat:VIA-0.6mm, F.Cu at (171.8, 91.0)
- added REF**: VIA-0.6mm, SFUSat:VIA-0.6mm, F.Cu at (158.8, 117.2)
- added REF**: VIA-0.6mm, SFUSat:VIA-0.6mm, F.Cu at (157.2, 117.2)
- added REF**: VIA-0.6mm, SFUSat:VIA-0.6mm, F.Cu at (155.8, 117.2)
- added REF**: VIA-0.6mm, SFUSat:VIA-0.6mm, F.Cu at (154.2, 117.2)
- added REF**: VIA-0.6mm, SFUSat:VIA-0.6mm, F.Cu at (152.8, 117.2)
- added REF**: VIA-0.6mm, SFUSat:VIA-0.6mm, F.Cu at (151.2, 117.2)
- added REF**: VIA-0.6mm, SFUSat:VIA-0.6mm, F.Cu at (197.8, 117.8)
- added REF**: VIA-0.6mm, SFUSat:VIA-0.6mm, F.Cu at (197.8, 119.2)
- added REF**: VIA-0.6mm, SFUSat:VIA-0.6mm, F.Cu at (197.8, 120.8)
- added REF**: VIA-0.6mm, SFUSat:VIA-0.6mm, F.Cu at (197.8, 122.2)
- added REF**: VIA-0.6mm, SFUSat:VIA-0.6mm, F.Cu at (168.8, 94.5)
- added REF**: VIA-0.6mm, SFUSat:VIA-0.6mm, F.Cu at (197.8, 123.8)
- added REF**: VIA-0.6mm, SFUSat:VIA-0.6mm, F.Cu at (197.8, 125.2)
- added REF**: VIA-0.6mm, SFUSat:VIA-0.6mm, F.Cu at (197.8, 126.8)
- added REF**: VIA-0.6mm, SFUSat:VIA-0.6mm, F.Cu at (197.8, 128.2)
- added REF**: VIA-0.6mm, SFUSat:VIA-0.6mm, F.Cu at (197.8, 129.8)
- added REF**: VIA-0.6mm, SFUSat:VIA-0.6mm, F.Cu at (197.8, 131.2)
- added REF**: VIA-0.6mm, SFUSat:VIA-0.6mm, F.Cu at (197.8, 132.8)
- added REF**: VIA-0.6mm, SFUSat:VIA-0.6mm, F.Cu at (197.8, 134.2)
- added REF**: VIA-0.6mm, SFUSat:VIA-0.6mm, F.Cu at (197.8, 135.8)
- added REF**: VIA-0.6mm, SFUSat:VIA-0.6mm, F.Cu at (197.8, 137.2)
- added REF**: VIA-0.6mm, SFUSat:VIA-0.6mm, F.Cu at (171.8, 88.0)
- added REF**: VIA-0.6mm, SFUSat:VIA-0.6mm, F.Cu at (197.8, 138.8)
- added REF**: VIA-0.6mm, SFUSat:VIA-0.6mm, F.Cu at (197.8, 140.2)
- added REF**: VIA-0.6mm, SFUSat:VIA-0.6mm, F.Cu at (197.8, 141.8)
- added REF**: VIA-0.6mm, SFUSat:VIA-0.6mm, F.Cu at (197.8, 143.2)
- added REF**: VIA-0.6mm, SFUSat:VIA-0.6mm, F.Cu at (197.8, 144.8)
- added REF**: VIA-0.6mm, SFUSat:VIA-0.6mm, F.Cu at (197.8, 146.2)
- added REF**: VIA-0.6mm, SFUSat:VIA-0.6mm, F.Cu at (197.8, 147.8)
- added REF**: VIA-0.6mm, SFUSat:VIA-0.6mm, F.Cu at (196.2, 147.8)
- added REF**: VIA-0.6mm, SFUSat:VIA-0.6mm, F.Cu at (194.8, 147.8)
- added REF**: VIA-0.6mm, SFUSat:VIA-0.6mm, F.Cu at (193.2, 147.8)
- added REF**: VIA-0.6mm, SFUSat:VIA-0.6mm, F.Cu at (168.8, 88.0)
- added REF**: VIA-0.6mm, SFUSat:VIA-0.6mm, F.Cu at (191.8, 147.8)
- added REF**: VIA-0.6mm, SFUSat:VIA-0.6mm, F.Cu at (190.2, 147.8)
- added REF**: VIA-0.6mm, SFUSat:VIA-0.6mm, F.Cu at (188.8, 147.8)
- added REF**: VIA-0.6mm, SFUSat:VIA-0.6mm, F.Cu at (187.2, 147.8)
- added REF**: VIA-0.6mm, SFUSat:VIA-0.6mm, F.Cu at (185.8, 147.8)
- added REF**: VIA-0.6mm, SFUSat:VIA-0.6mm, F.Cu at (184.2, 147.8)
- added REF**: VIA-0.6mm, SFUSat:VIA-0.6mm, F.Cu at (182.8, 147.8)
- added REF**: VIA-0.6mm, SFUSat:VIA-0.6mm, F.Cu at (181.2, 147.8)
- added REF**: VIA-0.6mm, SFUSat:VIA-0.6mm, F.Cu at (179.8, 147.8)
- added REF**: VIA-0.6mm, SFUSat:VIA-0.6mm, F.Cu at (178.2, 147.8)
- added mouse-bite-2mm-slot: VAL**, SFUSat:mouse-bite-2mm-slot, F.Cu at (150.0, 66.2)
- added mouse-bite-2mm-slot: VAL**, SFUSat:mouse-bite-2mm-slot, F.Cu at (150.0, 98.8)
- L6: value L -> 0R0
- moved J2 71.1 mm to (190.9, 102.0), turned to 90 degrees
- moved J13 66.0 mm to (191.2, 61.0), turned to 90 degrees
- moved U6 58.8 mm to (161.3, 77.9)
- moved U4 57.3 mm to (167.3, 82.1)
- moved U2 56.0 mm to (189.7, 85.5), turned to 90 degrees
- moved J5 54.4 mm to (180.5, 55.2), turned to 180 degrees
- moved U5 53.6 mm to (162.1, 91.6), turned to 0 degrees
- moved J14 53.2 mm to (187.0, 110.5), turned to 180 degrees
- moved D4 52.5 mm to (178.4, 97.9), turned to 90 degrees
- moved J8 50.9 mm to (174.0, 61.5)
- moved J12 50.0 mm to (113.8, 137.2)
- moved C34 50.0 mm to (177.9, 107.4)
- moved C1 49.1 mm to (183.2, 98.5), turned to 270 degrees
- moved C36 48.6 mm to (177.9, 102.1)
- moved C33 48.1 mm to (176.6, 111.6)
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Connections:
- RV1 pad 2: /3.1V -> /3V1
- U3 pad 8: /3.1V -> /3V1
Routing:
- net /3V6: track 0.00 -> 117.1 mm, vias 0 -> 2
- net /3V1: track 0.00 -> 60.7 mm
- net /PWR_SENSE: track 0.00 -> 50.3 mm, vias 0 -> 2
- net /G_DAC: track 0.00 -> 46.5 mm, vias 0 -> 1
- net /PWR_REF: track 0.00 -> 43.7 mm, vias 0 -> 2
- net /VREG: track 0.00 -> 42.9 mm, vias 0 -> 2
- net Net-(J6-Pad1): track 0.00 -> 35.5 mm, vias 0 -> 1
- net Net-(C33-Pad1): track 0.00 -> 22.1 mm
- net Net-(J7-Pad3): track 0.00 -> 20.3 mm, vias 0 -> 1
- net Net-(J5-Pad2): track 0.00 -> 18.7 mm, vias 0 -> 1
- net /G_MAN: track 0.00 -> 15.5 mm
- net Net-(C20-Pad1): track 0.00 -> 12.5 mm
- net GND: track 7.15 -> 17.1 mm
- net Net-(C16-Pad1): track 0.00 -> 8.87 mm
- net Net-(C26-Pad1): track 0.00 -> 7.99 mm
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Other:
- outline, holes or cut-outs redrawn
- net class Digital added: clearance 0.2, trace_width 0.25, via_dia 0.6, via_drill 0.4
- board text added: "3V1"
- board text added: "3V6"
- board text added: "G_DAC"
- board text added: "G_MAN"
- board text added: "PWR_REF"
- board text added: "PWR_SENSE"
- board text added: "VREG"
